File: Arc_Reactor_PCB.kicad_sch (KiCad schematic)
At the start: 40 parts, among them J1 Conn_01x01, J2 Conn_01x01, J3 USB_C_Receptacle, J4 Conn_01x03, SW1 SW_Push, SW2 SW_Push, U1 ESP32-C3-MINI-1, U2 AP63205WU, U3 SN74AHCT1G125, U4 LM66200DRLR, U5 AP2112K-3.3

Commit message: Updates
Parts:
- L1: LCSC C57269 -> C167874
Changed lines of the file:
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@@
 			)
 		)
-		(property "LCSC" "C57269"
+		(property "LCSC" "C167874"
 			(at 223.52 97.79 90)
 			(hide yes)

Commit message: Updates for production
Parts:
- C10, C3, C9: footprint Capacitor_SMD:C_0402_1005Metric -> Capacitor_SMD:C_0603_1608Metric; LCSC C52923 -> C90540
- J1, J2: now not fitted
- L1: footprint SWPA4030S4R7MT:IND-SMD_L4.0-W4.0 -> FNR4030S4R7MT:IND-SMD_L4.0-W4.0_FNR40XXS
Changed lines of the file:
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@@
 			)
 		)
-		(property "Footprint" "Capacitor_SMD:C_0402_1005Metric"
+		(property "Footprint" "Capacitor_SMD:C_0603_1608Metric"
 			(at 233.3752 140.97 0)
 			(hide yes)
@@
 			)
 		)
-		(property "LCSC" "C52923"
+		(property "LCSC" "C90540"
 			(at 232.41 144.78 0)
 			(hide yes)
@@
 		(on_board yes)
 		(in_pos_files yes)
-		(dnp no)
+		(dnp yes)
 		(fields_autoplaced yes)
 		(property "Reference" "J2"
@@
 			)
 		)
-		(property "Footprint" "Capacitor_SMD:C_0402_1005Metric"
+		(property "Footprint" "Capacitor_SMD:C_0603_1608Metric"
 			(at 36.5252 48.26 0)
 			(hide yes)
@@
 			)
 		)
-		(property "LCSC" "C52923"
+		(property "LCSC" "C90540"
 			(at 35.56 52.07 0)
 			(hide yes)
@@
 		(on_board yes)
 		(in_pos_files yes)
-		(dnp no)
+		(dnp yes)
 		(fields_autoplaced yes)
 		(property "Reference" "J1"
@@
 			)
 		)
-		(property "Footprint" "Capacitor_SMD:C_0402_1005Metric"
+		(property "Footprint" "Capacitor_SMD:C_0603_1608Metric"
 			(at 260.6548 140.97 0)
 			(hide yes)
@@
 			)
 		)
-		(property "LCSC" "C52923"
+		(property "LCSC" "C90540"
 			(at 261.62 144.78 0)
 			(hide yes)
@@
 			)
 		)
-		(property "Footprint" "SWPA4030S4R7MT:IND-SMD_L4.0-W4.0"
+		(property "Footprint" "FNR4030S4R7MT:IND-SMD_L4.0-W4.0_FNR40XXS"
 			(at 223.52 97.79 0)
 			(hide yes)

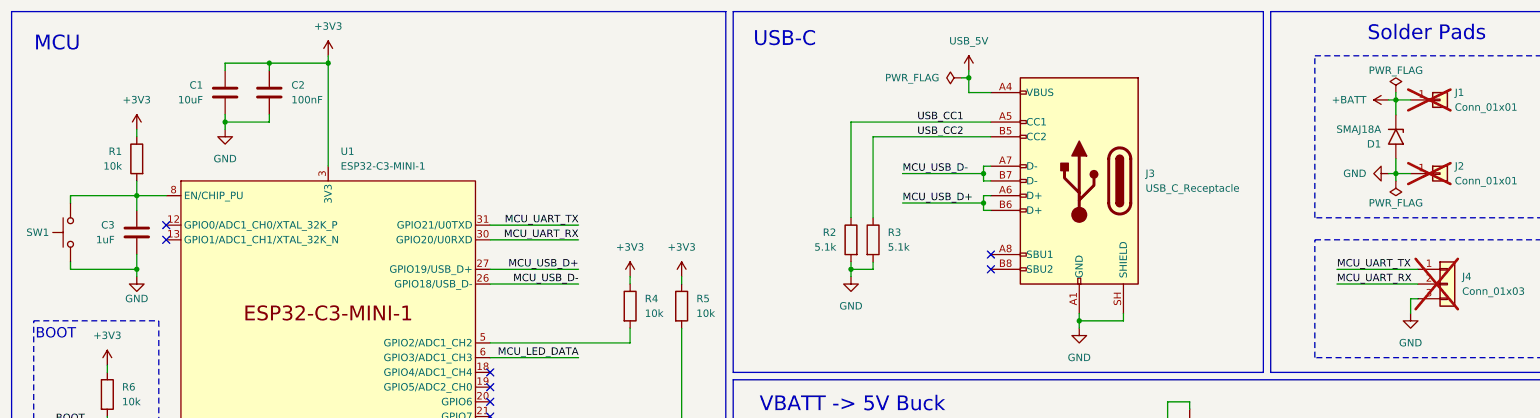
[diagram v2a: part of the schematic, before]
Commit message: Improve placement/routing
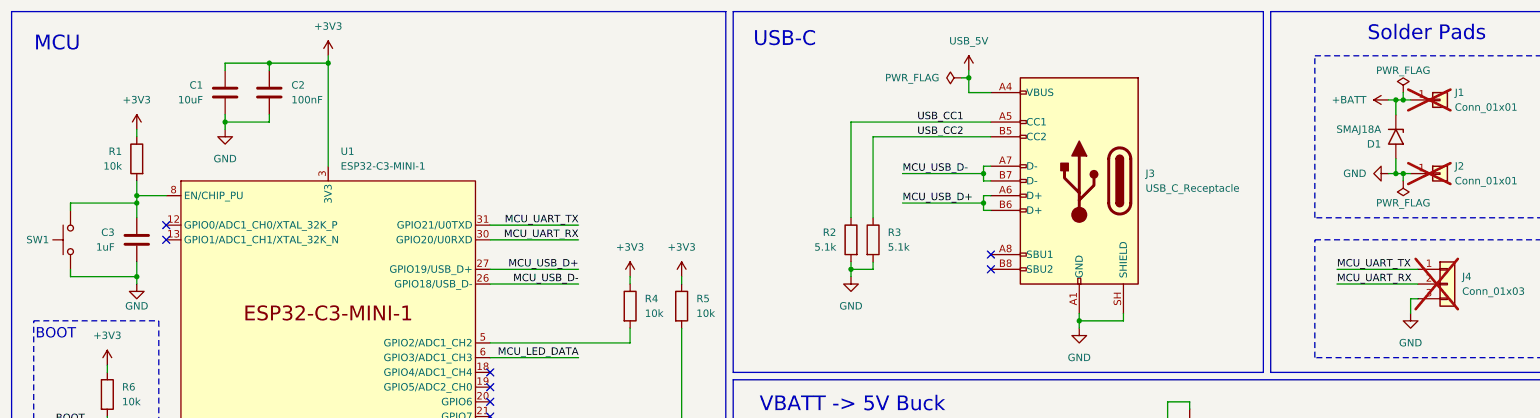
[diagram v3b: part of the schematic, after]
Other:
- moved on the sheet: C3, SW1
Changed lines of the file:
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@@
 	)
 	(junction
+		(at 35.56 46.99)
+		(diameter 0)
+		(color 0 0 0 0)
+	)
+	(junction
 		(at 246.38 96.52)
 		(diameter 0)
@@
 	)
 	(junction
-		(at 35.56 158.75)
+		(at 254 29.21)
 		(diameter 0)
 		(color 0 0 0 0)
 	)
 	(junction
-		(at 217.17 97.79)
+		(at 35.56 158.75)
 		(diameter 0)
 		(color 0 0 0 0)
 	)
 	(junction
-		(at 35.56 58.42)
+		(at 217.17 97.79)
 		(diameter 0)
 		(color 0 0 0 0)
@@
 		(color 0 0 0 0)
 	)
+	(junction
+		(at 254 41.91)
+		(diameter 0)
+		(color 0 0 0 0)
+	)
+	(junction
+		(at 35.56 59.69)
+		(diameter 0)
+		(color 0 0 0 0)
+	)
 	(no_connect
 		(at 96.52 81.28)
@@
 	(wire
 		(pts
-			(xy 252.73 41.91) (xy 252.73 43.18)
+			(xy 254 41.91) (xy 254 43.18)
 		)
 		(stroke
@@
 	(wire
 		(pts
+			(xy 35.56 46.99) (xy 35.56 49.53)
+		)
+		(stroke
+			(width 0)
+			(type default)
+		)
+	)
+	(wire
+		(pts
 			(xy 96.52 73.66) (xy 111.76 73.66)
 		)
@@
 	(wire
 		(pts
+			(xy 254 29.21) (xy 255.27 29.21)
+		)
+		(stroke
+			(width 0)
+			(type default)
+		)
+	)
+	(wire
+		(pts
 			(xy 88.9 142.24) (xy 88.9 140.97)
 		)
@@
 	(wire
 		(pts
-			(xy 24.13 57.15) (xy 24.13 58.42)
+			(xy 24.13 58.42) (xy 24.13 59.69)
 		)
 		(stroke
@@
 	(wire
 		(pts
-			(xy 24.13 45.72) (xy 35.56 45.72)
+			(xy 24.13 46.99) (xy 35.56 46.99)
+		)
+		(stroke
+			(width 0)
+			(type default)
+		)
+	)
+	(wire
+		(pts
+			(xy 254 41.91) (xy 252.73 41.91)
 		)
 		(stroke
@@
 	(wire
 		(pts
-			(xy 252.73 29.21) (xy 255.27 29.21)
+			(xy 252.73 29.21) (xy 254 29.21)
 		)
 		(stroke
@@
 	(wire
 		(pts
-			(xy 35.56 59.69) (xy 35.56 58.42)
+			(xy 35.56 60.96) (xy 35.56 59.69)
 		)
 		(stroke
@@
 	(wire
 		(pts
-			(xy 24.13 46.99) (xy 24.13 45.72)
+			(xy 24.13 48.26) (xy 24.13 46.99)
 		)
 		(stroke
@@
 	(wire
 		(pts
-			(xy 252.73 41.91) (xy 255.27 41.91)
+			(xy 35.56 45.72) (xy 35.56 46.99)
 		)
 		(stroke
@@
 	(wire
 		(pts
-			(xy 35.56 45.72) (xy 35.56 48.26)
+			(xy 35.56 157.48) (xy 35.56 158.75)
 		)
 		(stroke
@@
 	(wire
 		(pts
-			(xy 35.56 157.48) (xy 35.56 158.75)
+			(xy 181.61 46.99) (xy 181.61 45.72)
 		)
 		(stroke
@@
 	(wire
 		(pts
-			(xy 181.61 46.99) (xy 181.61 45.72)
+			(xy 255.27 63.5) (xy 256.54 63.5)
 		)
 		(stroke
@@
 	(wire
 		(pts
-			(xy 255.27 63.5) (xy 256.54 63.5)
+			(xy 254 41.91) (xy 255.27 41.91)
 		)
 		(stroke
@@
 	(wire
 		(pts
-			(xy 252.73 27.94) (xy 252.73 29.21)
+			(xy 254 27.94) (xy 254 29.21)
 		)
 		(stroke
@@
 	(wire
 		(pts
+			(xy 35.56 57.15) (xy 35.56 59.69)
+		)
+		(stroke
+			(width 0)
+			(type default)
+		)
+	)
+	(wire
+		(pts
 			(xy 88.9 140.97) (xy 115.57 140.97)
 		)
@@
 	(wire
 		(pts
-			(xy 24.13 58.42) (xy 35.56 58.42)
+			(xy 24.13 59.69) (xy 35.56 59.69)
 		)
 		(stroke
@@
 	(wire
 		(pts
-			(xy 35.56 55.88) (xy 35.56 58.42)
-		)
-		(stroke
-			(width 0)
-			(type default)
-		)
-	)
-	(wire
-		(pts
 			(xy 120.65 59.69) (xy 120.65 60.96)
 		)
@@
 	(symbol
 		(lib_id "power:PWR_FLAG")
-		(at 252.73 43.18 180)
+		(at 254 43.18 180)
 		(unit 1)
 		(body_style 1)
@@
 		(dnp no)
 		(property "Reference" "#FLG03"
-			(at 252.73 45.085 0)
+			(at 254 45.085 0)
 			(hide yes)
 			(show_name no)
@@
 		)
 		(property "Value" "PWR_FLAG"
-			(at 252.73 46.99 0)
+			(at 254 46.99 0)
 			(show_name no)
 			(do_not_autoplace no)
@@
 		)
 		(property "Footprint" ""
-			(at 252.73 43.18 0)
+			(at 254 43.18 0)
 			(hide yes)
 			(show_name no)
@@
 		)
 		(property "Datasheet" ""
-			(at 252.73 43.18 0)
+			(at 254 43.18 0)
 			(hide yes)
 			(show_name no)
@@
 		)
 		(property "Description" "Special symbol for telling ERC where power comes from"
-			(at 252.73 43.18 0)
+			(at 254 43.18 0)
 			(hide yes)
 			(show_name no)
@@
 	(symbol
 		(lib_id "Device:C")
-		(at 35.56 52.07 0)
+		(at 35.56 53.34 0)
 		(mirror x)
 		(unit 1)
@@
 		(fields_autoplaced yes)
 		(property "Reference" "C3"
-			(at 31.75 50.7999 0)
+			(at 31.75 52.0699 0)
 			(show_name no)
 			(do_not_autoplace no)
@@
 		)
 		(property "Value" "1uF"
-			(at 31.75 53.3399 0)
+			(at 31.75 54.6099 0)
 			(show_name no)
 			(do_not_autoplace no)
@@
 		)
 		(property "Footprint" "Capacitor_SMD:C_0603_1608Metric"
-			(at 36.5252 48.26 0)
+			(at 36.5252 49.53 0)
 			(hide yes)
 			(show_name no)
@@
 		)
 		(property "Datasheet" ""
-			(at 35.56 52.07 0)
+			(at 35.56 53.34 0)
 			(hide yes)
 			(show_name no)
@@
 		)
 		(property "Description" "Unpolarized capacitor"
-			(at 35.56 52.07 0)
+			(at 35.56 53.34 0)
 			(hide yes)
 			(show_name no)
@@
 		)
 		(property "LCSC" "C90540"
-			(at 35.56 52.07 0)
+			(at 35.56 53.34 0)
 			(hide yes)
 			(show_name no)
@@
 	(symbol
 		(lib_id "power:PWR_FLAG")
-		(at 252.73 27.94 0)
+		(at 254 27.94 0)
 		(mirror y)
 		(unit 1)
@@
 		(dnp no)
 		(property "Reference" "#FLG02"
-			(at 252.73 26.035 0)
+			(at 254 26.035 0)
 			(hide yes)
 			(show_name no)
@@
 		)
 		(property "Value" "PWR_FLAG"
-			(at 252.73 24.13 0)
+			(at 254 24.13 0)
 			(show_name no)
 			(do_not_autoplace no)
@@
 		)
 		(property "Footprint" ""
-			(at 252.73 27.94 0)
+			(at 254 27.94 0)
 			(hide yes)
 			(show_name no)
@@
 		)
 		(property "Datasheet" ""
-			(at 252.73 27.94 0)
+			(at 254 27.94 0)
 			(hide yes)
 			(show_name no)
@@
 		)
 		(property "Description" "Special symbol for telling ERC where power comes from"
-			(at 252.73 27.94 0)
+			(at 254 27.94 0)
 			(hide yes)
 			(show_name no)
@@
 	(symbol
 		(lib_id "power:GND")
-		(at 35.56 59.69 0)
+		(at 35.56 60.96 0)
 		(unit 1)
 		(body_style 1)
@@
 		(dnp no)
 		(property "Reference" "#PWR07"
-			(at 35.56 66.04 0)
+			(at 35.56 67.31 0)
 			(hide yes)
 			(show_name no)
@@
 		)
 		(property "Value" "GND"
-			(at 35.56 63.5 0)
+			(at 35.56 64.77 0)
 			(show_name no)
 			(do_not_autoplace no)
@@
 		)
 		(property "Footprint" ""
-			(at 35.56 59.69 0)
+			(at 35.56 60.96 0)
 			(hide yes)
 			(show_name no)
@@
 		)
 		(property "Datasheet" ""
-			(at 35.56 59.69 0)
+			(at 35.56 60.96 0)
 			(hide yes)
 			(show_name no)
@@
 		)
 		(property "Description" "Power symbol creates a global label with name \"GND\" , ground"
-			(at 35.56 59.69 0)
+			(at 35.56 60.96 0)
 			(hide yes)
 			(show_name no)
@@
 	(symbol
 		(lib_id "Switch:SW_Push")
-		(at 24.13 52.07 90)
+		(at 24.13 53.34 90)
 		(unit 1)
 		(body_style 1)
@@
 		(dnp no)
 		(property "Reference" "SW1"
-			(at 16.51 52.07 90)
+			(at 16.51 53.34 90)
 			(show_name no)
 			(do_not_autoplace no)
@@
 		)
 		(property "Value" "SW_Push"
-			(at 12.192 53.086 90)
+			(at 12.192 54.356 90)
 			(hide yes)
 			(show_name no)
@@
 		)
 		(property "Footprint" "Button_Switch_SMD:SW_SPST_TS-1088-xR020"
-			(at 19.05 52.07 0)
+			(at 19.05 53.34 0)
 			(hide yes)
 			(show_name no)
@@
 		)
 		(property "Datasheet" ""
-			(at 19.05 52.07 0)
+			(at 19.05 53.34 0)
 			(hide yes)
 			(show_name no)
@@
 		)
 		(property "Description" "Push button switch, generic, two pins"
-			(at 24.13 52.07 0)
+			(at 24.13 53.34 0)
 			(hide yes)
 			(show_name no)
@@
 		)
 		(property "LCSC" "C720477"
-			(at 24.13 52.07 90)
+			(at 24.13 53.34 90)
 			(hide yes)
 			(show_name no)

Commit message: Add SMAJ5.0A TVS on USB VBUS
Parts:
- added D2: SMAJ5.0A, Diode_SMD:D_SMA, symbol Diode:SMAJ5.0A
- renumbered D9 to D10, D10 to D11, D2 to D3, D3 to D4, D4 to D5, D5 to D6, D6 to D7, D7 to D8, D8 to D9
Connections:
- net GND: now also D2.2 (A2)
- net USB_5V: now also D2.1 (A1)
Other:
- moved on the sheet: J3, R2, R3

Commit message: Update BOM
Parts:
- C7: LCSC C15850 -> C318691
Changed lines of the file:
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@@
 			)
 		)
-		(property "LCSC" "C15850"
+		(property "LCSC" "C318691"
 			(at 177.8 104.14 0)
 			(hide yes)
